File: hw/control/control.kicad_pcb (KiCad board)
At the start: 2 copper layers, 160 x 90 mm, 143 parts, among them J101 Screw_Terminal_01x02, J102 Screw_Terminal_01x03, J103 Screw_Terminal_01x03, J301 Conn_02x05_Odd_Even, J302 Conn_01x04, J303 Raspberry_Pi_0_2_3, J304 Micro_SD_Card, J305 Conn_01x06, Q1001 BC807, Q1002 BC817, Q401 BC817, Q501 BC817, Q601 BC817, Q701 BC817, Q801 BC807, Q802 BC817, Q901 AOSP21357, Q902 IRF4905, U1001 LM2678T-ADJ, U1101 SN74AHCT125D, U201 LM2596T-ADJ, U801 LM2678T-ADJ

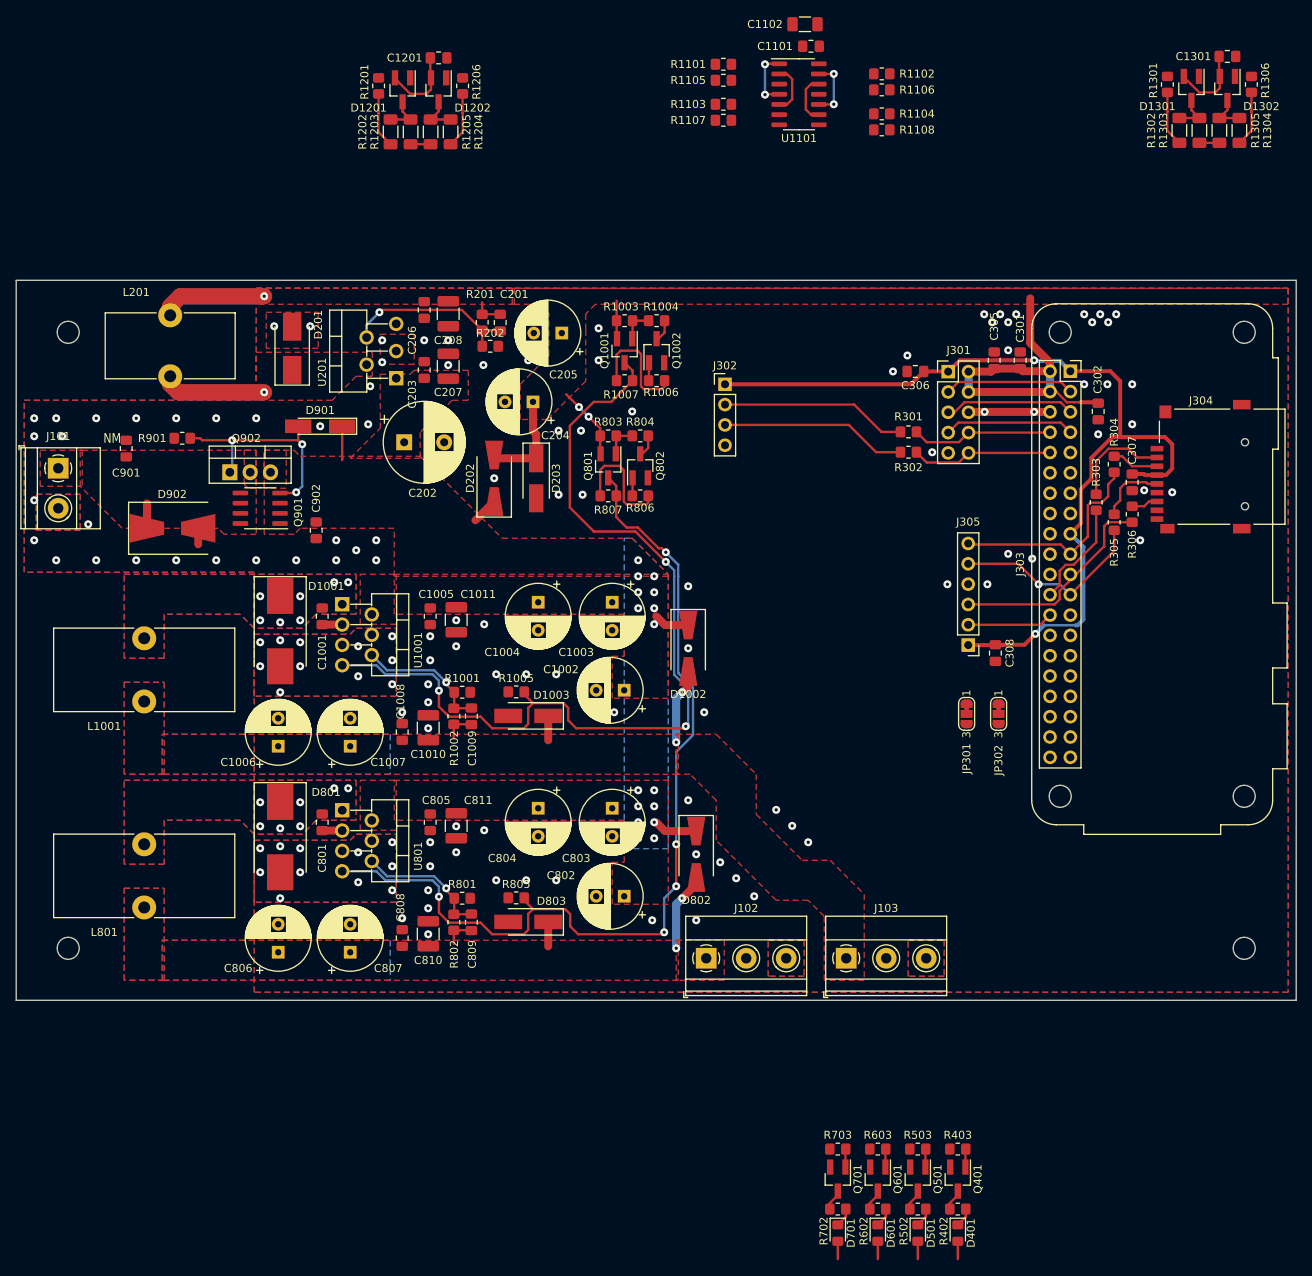
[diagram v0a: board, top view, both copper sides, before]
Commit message: [hw] Add control board's indication LEDs layout
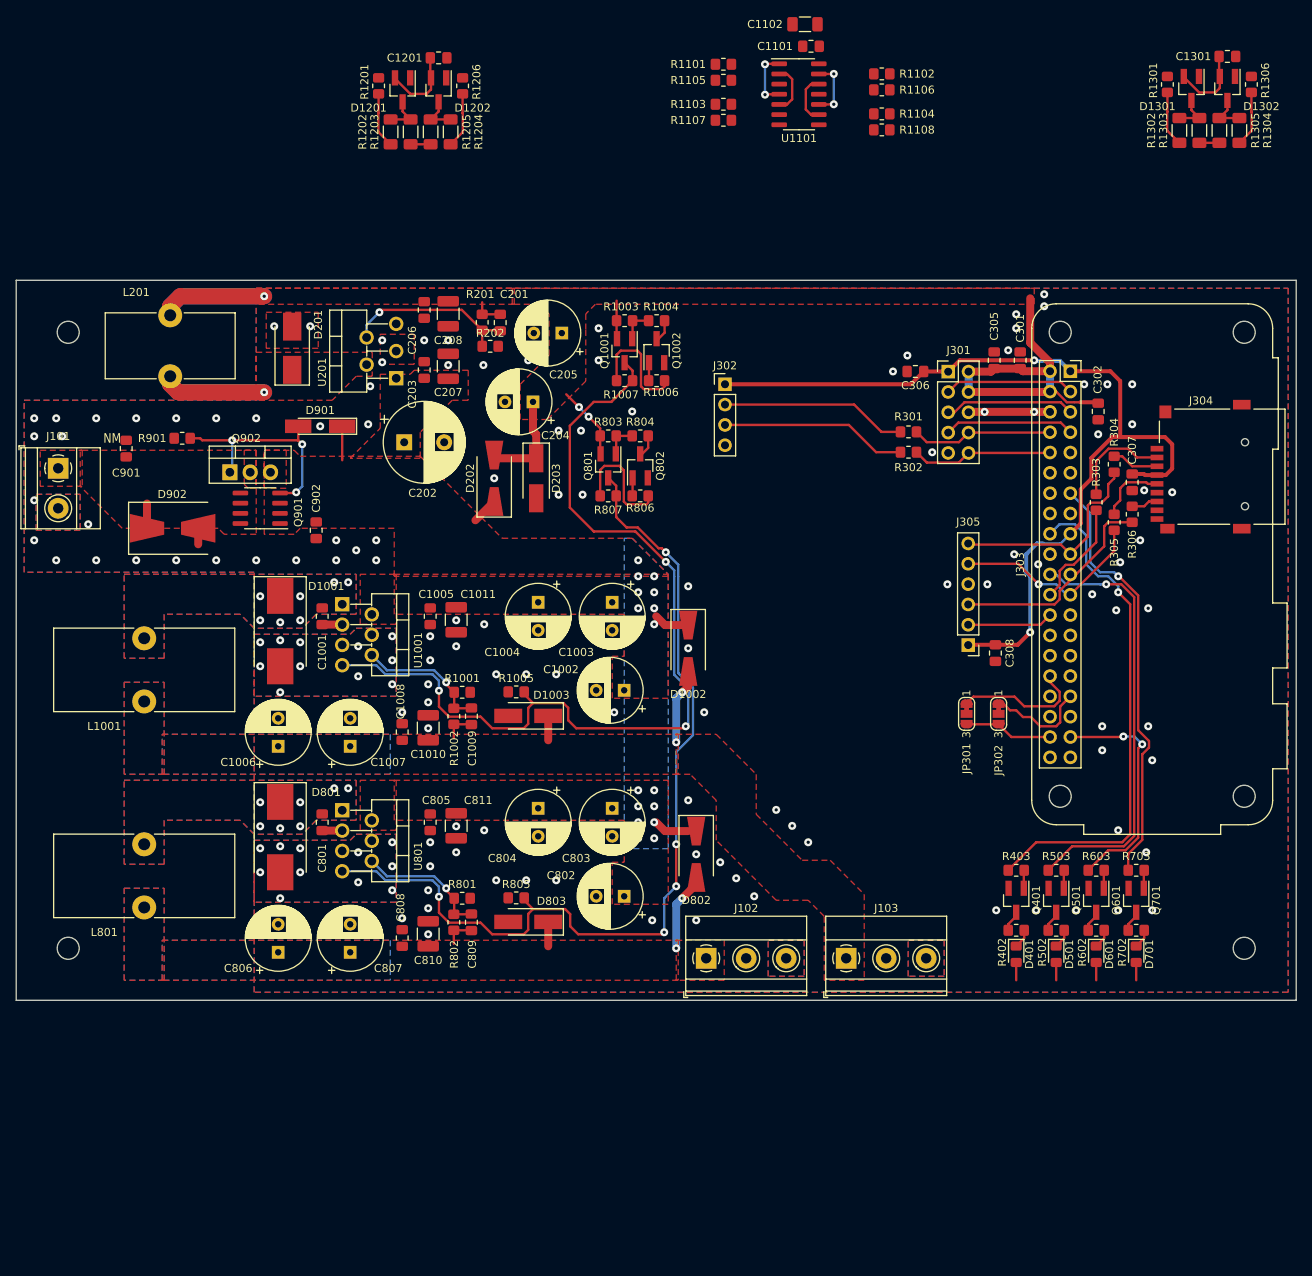
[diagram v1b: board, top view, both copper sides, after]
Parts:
- moved D701 51.0 mm to (200.0, 134.2)
- moved Q701 51.0 mm to (200.0, 127.5)
- moved R702 51.0 mm to (200.0, 131.2)
- moved R703 51.0 mm to (200.0, 123.8)
- moved D601 44.3 mm to (195.0, 134.2)
- moved Q601 44.3 mm to (195.0, 127.5)
- moved R602 44.3 mm to (195.0, 131.2)
- moved R603 44.3 mm to (195.0, 123.8)
- moved D501 38.9 mm to (190.0, 134.2)
- moved Q501 38.9 mm to (190.0, 127.5)
- moved R502 38.9 mm to (190.0, 131.2)
- moved R503 38.9 mm to (190.0, 123.8)
- moved D401 35.6 mm to (185.0, 134.2)
- moved Q401 35.6 mm to (185.0, 127.5)
- moved R402 35.6 mm to (185.0, 131.2)
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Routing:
- net /CPU/Status LED 0/IN_3V3: track 0.00 -> 63.1 mm, vias 0 -> 1
- net /CPU/Status LED 1/IN_3V3: track 0.00 -> 54.1 mm, vias 0 -> 1
- net /CPU/Status LED 3/IN_3V3: track 0.00 -> 53.4 mm, vias 0 -> 1
- net /CPU/Status LED 2/IN_3V3: track 0.00 -> 29.2 mm, vias 0 -> 2
- net Net-(J303-Pad32): track 0.00 -> 16.4 mm
- net Net-(J303-Pad33): track 0.00 -> 12.9 mm
- net /CPU/ALT_LED_DATA: track 0.00 -> 11.1 mm
- net +3V3: track 118.2 -> 116.1 mm
- net GND: vias 133 -> 142

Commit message: [hw] Add control LED data out stage layout
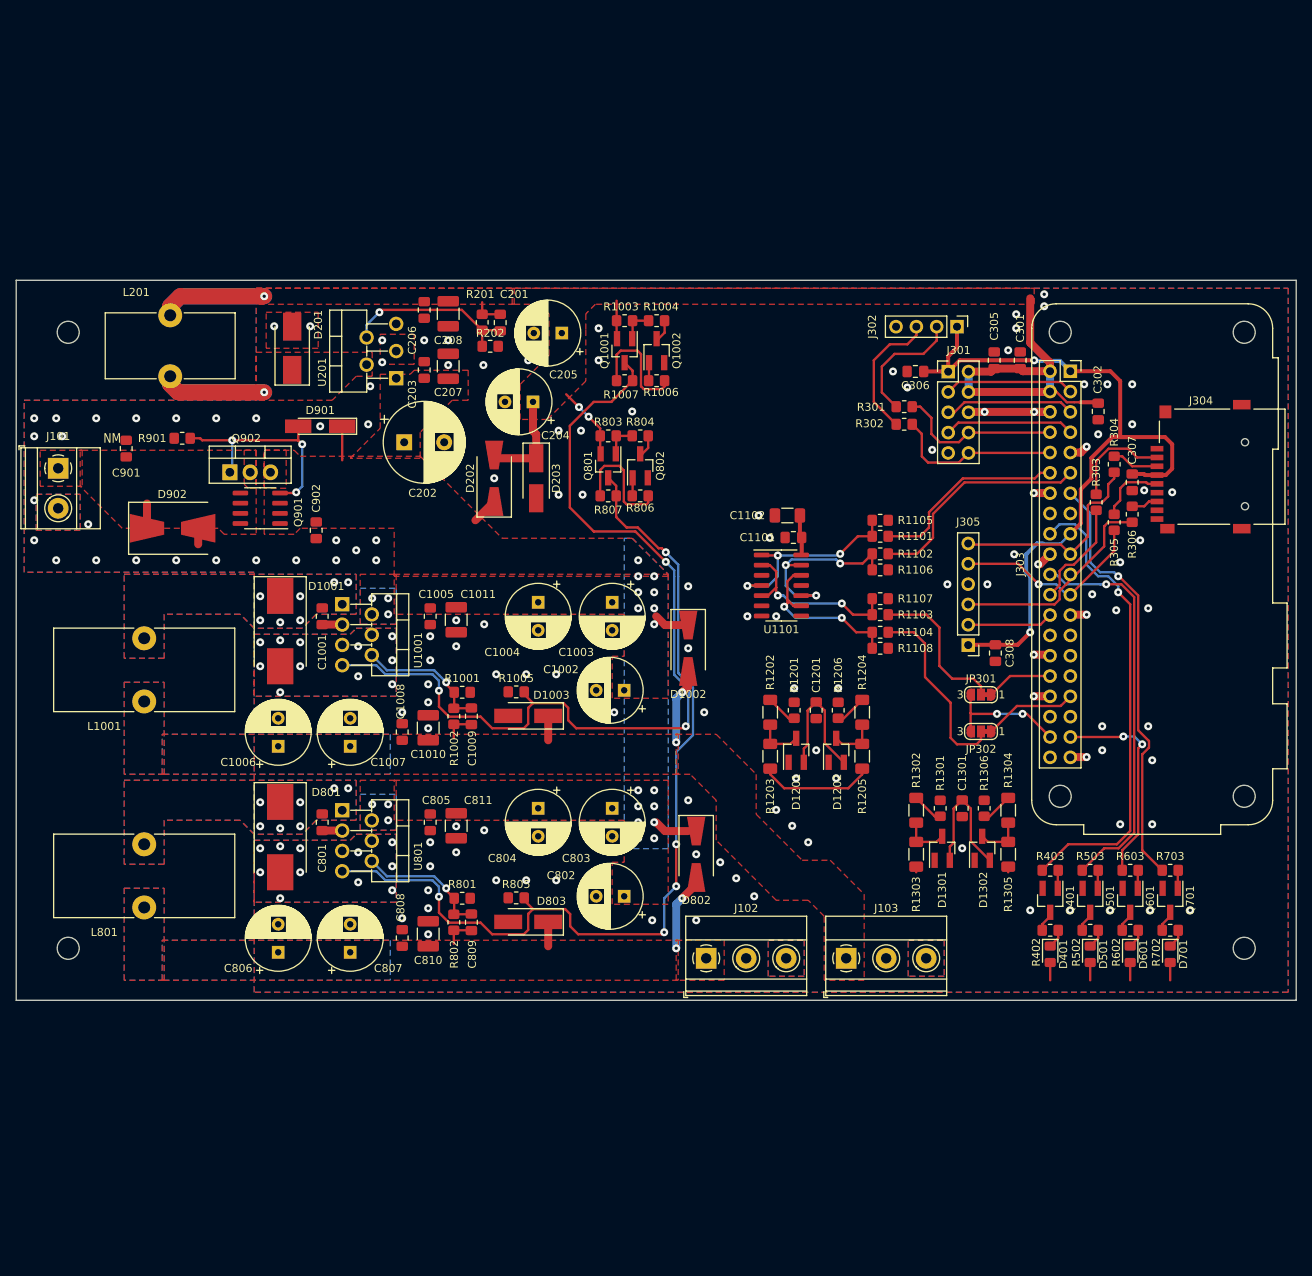
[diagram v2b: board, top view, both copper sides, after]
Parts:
- moved D1301 100.0 mm to (175.8, 121.0), turned to 90 degrees
- moved D1302 99.8 mm to (180.8, 121.0), turned to 90 degrees
- moved C1301 99.7 mm to (178.2, 116.0), turned to 270 degrees
- moved R1303 97.2 mm to (172.5, 121.8)
- moved R1306 96.4 mm to (181.0, 116.0)
- moved D1202 96.4 mm to (162.5, 108.8), turned to 90 degrees
- moved D1201 96.1 mm to (157.5, 108.8), turned to 90 degrees
- moved R1205 94.9 mm to (165.8, 109.5)
- moved R1301 94.8 mm to (175.5, 116.0)
- moved R1305 94.3 mm to (184.0, 121.8)
- moved C1201 94.2 mm to (160.0, 103.8), turned to 270 degrees
- moved R1201 93.8 mm to (157.2, 103.8)
- moved R1302 91.1 mm to (172.5, 116.2), turned to 90 degrees
- moved R1206 91.1 mm to (162.8, 103.8)
- moved R1203 90.1 mm to (154.2, 109.5)
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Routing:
- net /LED_DATA_~EN~1: track 0.00 -> 28.7 mm
- net /LED_DATA_~EN~0: track 0.00 -> 24.6 mm
- net /LED_DATA1: track 0.00 -> 23.7 mm
- net +5V: track 128.3 -> 148.5 mm
- net +3V3: track 116.1 -> 96.6 mm
- net /LED_DATA0: track 0.00 -> 19.2 mm
- net Net-(R1101-Pad1): track 7.40 -> 25.5 mm, vias 2 -> 3
- net Net-(R1102-Pad1): track 7.56 -> 24.5 mm, vias 2 -> 3
- net GND: track 12.2 -> 28.8 mm, vias 142 -> 158
- net Net-(R1103-Pad2): track 6.30 -> 22.3 mm, vias 0 -> 2
- net Net-(R1104-Pad1): track 6.30 -> 21.7 mm, vias 0 -> 2
- net /LED Driver/DATA_OUT0: track 2.50 -> 14.3 mm
- net Net-(J303-Pad32): track 16.4 -> 8.30 mm
- net Net-(J302-Pad2): track 23.3 -> 15.7 mm
- net Net-(J302-Pad3): track 23.3 -> 16.9 mm
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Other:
- net class Driver Signal: clearance 0.5 -> 0.3

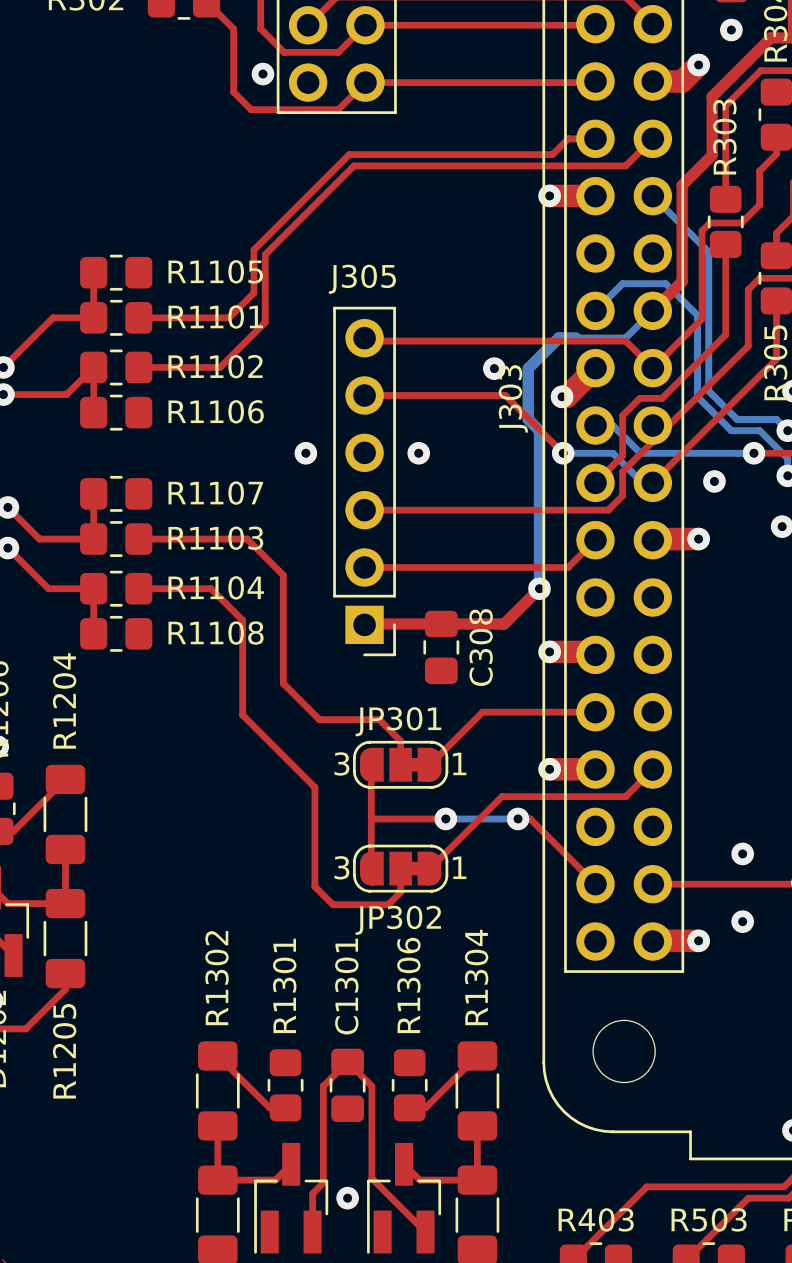
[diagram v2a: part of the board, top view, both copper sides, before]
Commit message: i[hw] Add IIS audio module connector
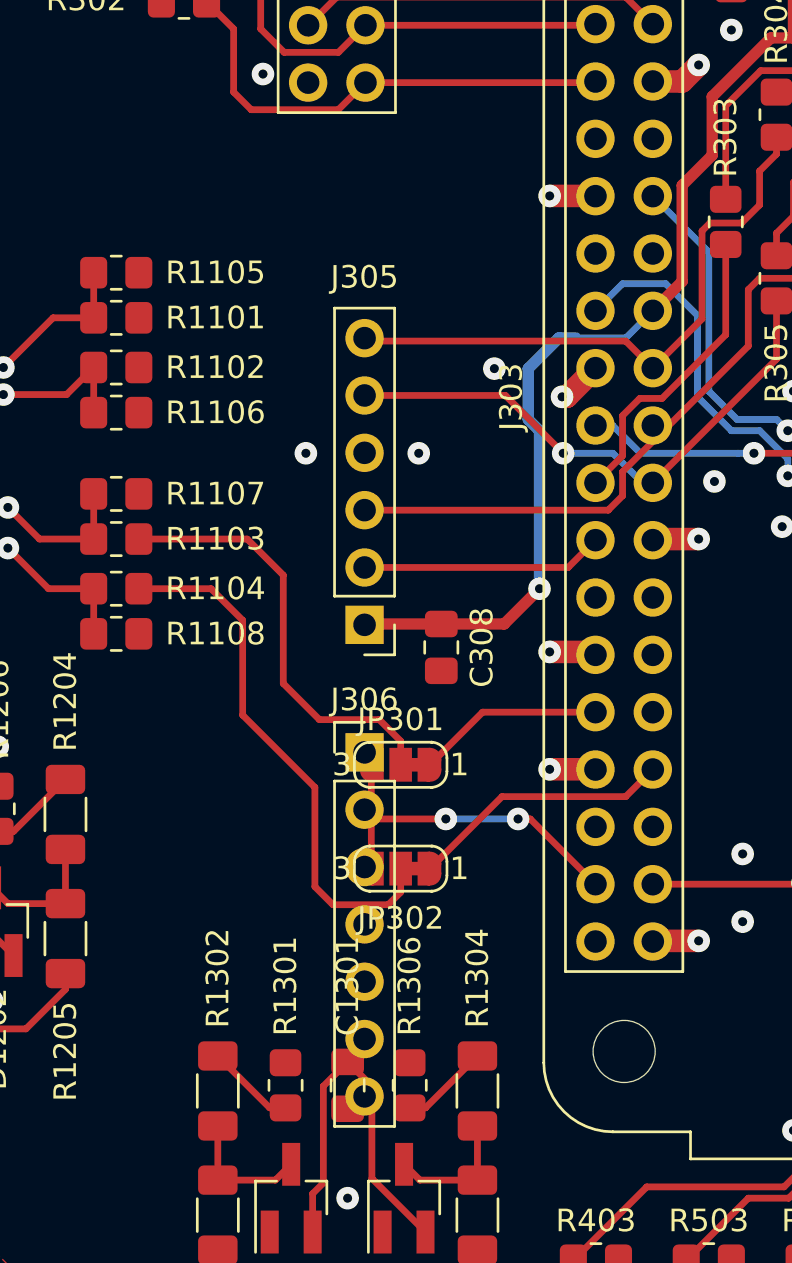
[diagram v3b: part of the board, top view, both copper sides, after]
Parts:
- added J306: Conn_01x07, Connector_PinHeader_2.54mm:PinHeader_1x07_P2.54mm_Vertical, F.Cu at (179.0, 101.2)
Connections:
- J303 pad 11: /LED_DATA_~EN~1 -> /LED_DATA_~EN~0
- J303 pad 12: /LED_DATA_~EN~0 -> /CPU/IIS_BCLK
- J303 pad 35: Net-(J303-Pad35) -> /CPU/IIS_LRC
- J303 pad 36: Net-(J303-Pad36) -> /LED_DATA_~EN~1
- J303 pad 40: Net-(J303-Pad40) -> /CPU/IIS_DIN
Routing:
- net /LED_DATA_~EN~1: track 28.7 -> 0.00 mm
- net /LED_DATA_~EN~0: track 24.6 -> 0.00 mm
